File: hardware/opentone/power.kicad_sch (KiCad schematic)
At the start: 32 parts

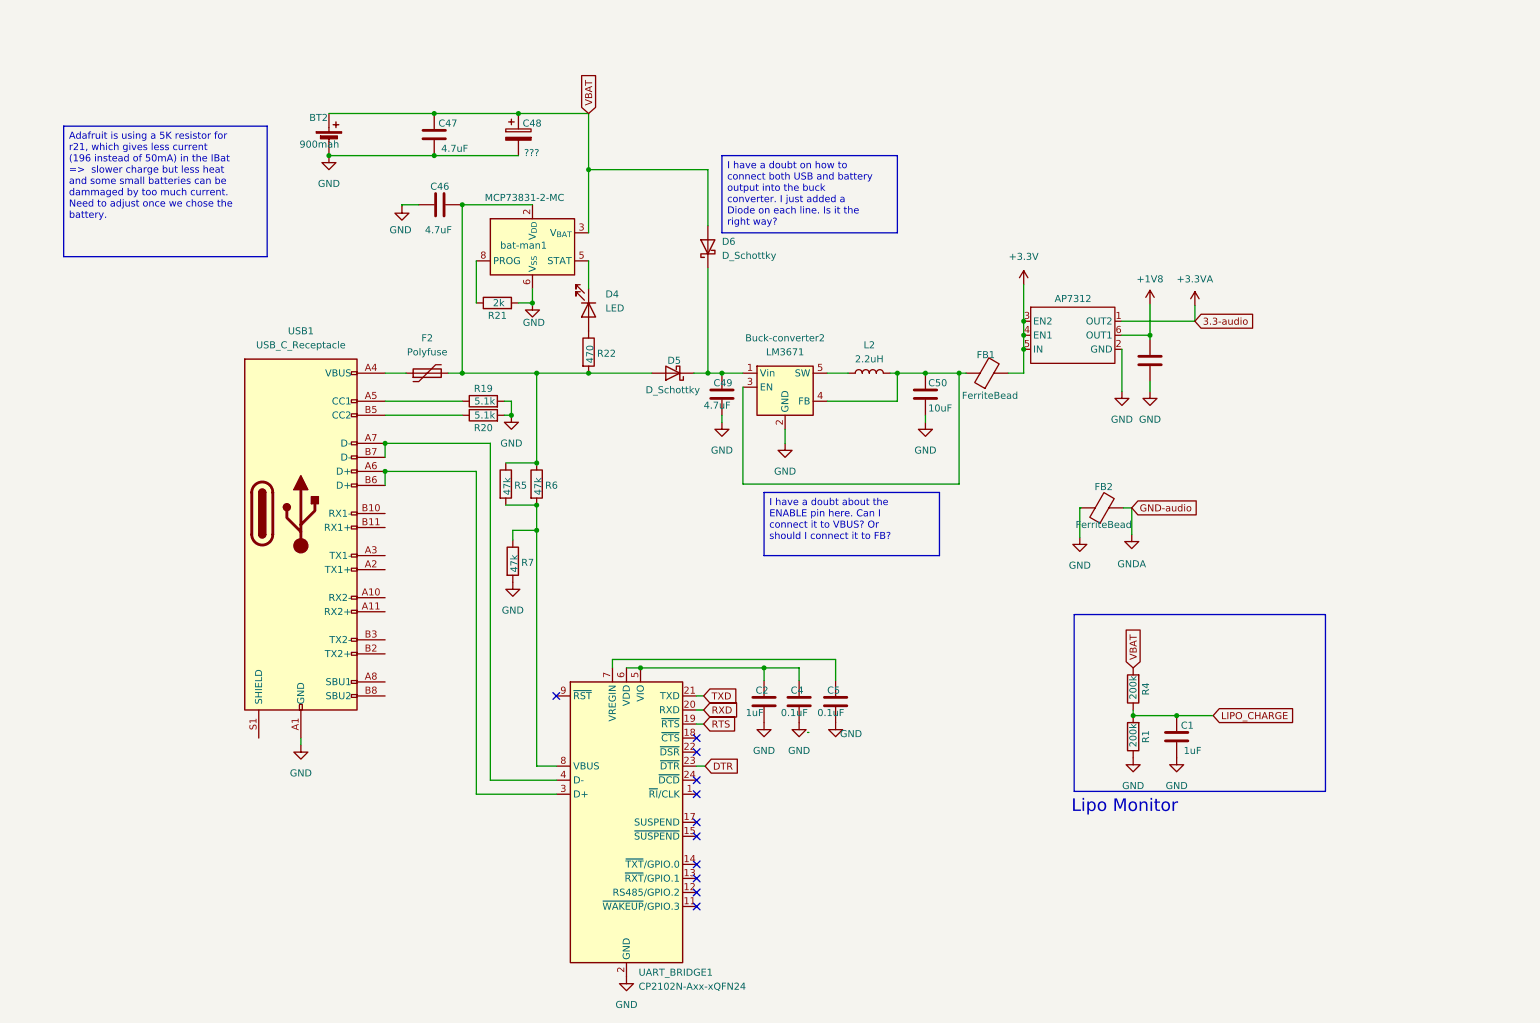
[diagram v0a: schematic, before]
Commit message: reworked power schematics
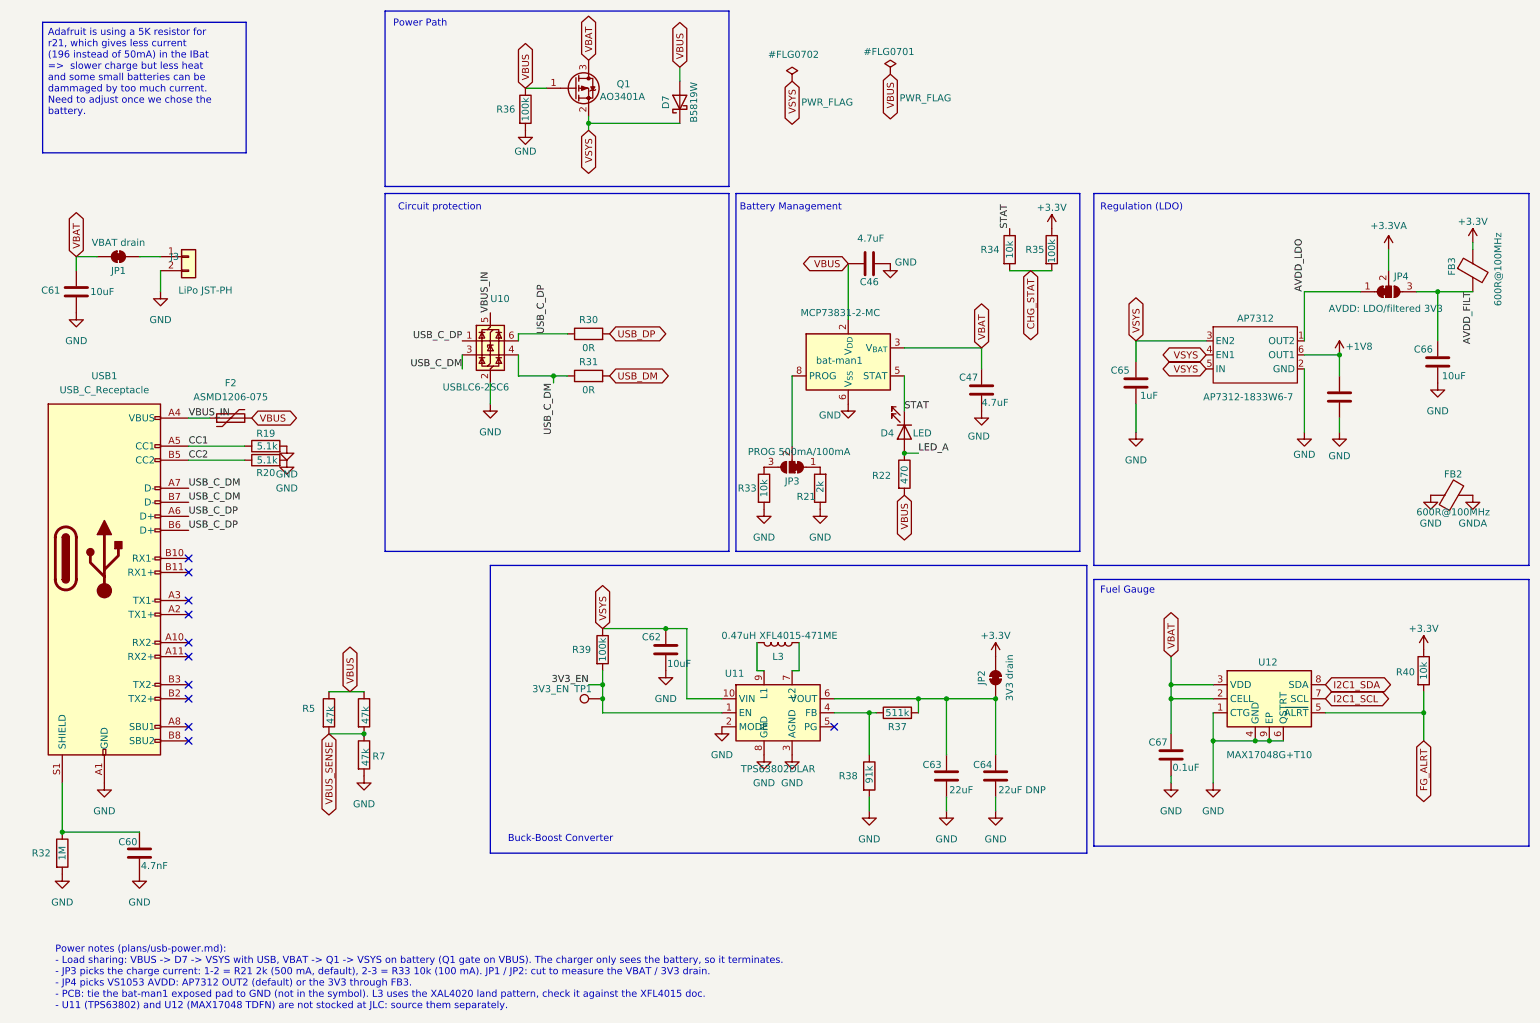
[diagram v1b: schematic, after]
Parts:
- removed BT2: 900mah, symbol Device:Battery_Cell
- removed Buck-converter2: LM3671, Package_TO_SOT_SMD:TSOT-23-5, symbol Regulator_Switching:LM3670MF
- removed C1, C2: 1uF, symbol Device:C
- removed C4, C5: 0.1uF, symbol Device:C
- removed C48: ???, symbol Device:C_Polarized
- removed C49: 4.7uF, symbol Device:C
- removed C50: 10uF, symbol Device:C
- removed D5, D6: D_Schottky, symbol Device:D_Schottky
- removed FB1: FerriteBead, symbol Device:FerriteBead
- removed L2: 2.2uH, symbol Device:L
- removed R1, R4: 200k, symbol Device:R
- removed UART_BRIDGE1: CP2102N-Axx-xQFN24, Package_DFN_QFN:QFN-24-1EP_4x4mm_P0.5mm_EP2.6x2.6mm, symbol Interface_USB:CP2102N-Axx-xQFN24
- added C60: 4.7nF, Capacitor_SMD:C_0805_2012Metric, symbol Device:C
- added C61, C62, C66: 10uF, Capacitor_SMD:C_0805_2012Metric, symbol Device:C
- added C63: 22uF, Capacitor_SMD:C_0805_2012Metric, symbol Device:C
- added C64: 22uF DNP, Capacitor_SMD:C_0805_2012Metric, symbol Device:C
- added C65: 1uF, Capacitor_SMD:C_0805_2012Metric, symbol Device:C
- added C67: 0.1uF, Capacitor_SMD:C_0805_2012Metric, symbol Device:C
- added D7: B5819W, Diode_SMD:D_SOD-123, symbol Device:D_Schottky
- added FB3: 600R@100MHz, Inductor_SMD:L_0805_2012Metric, symbol Device:FerriteBead
- added J3: LiPo JST-PH, Connector_JST:JST_PH_S2B-PH-SM4-TB_1x02-1MP_P2.00mm_Horizontal, symbol Connector_Generic:Conn_01x02
- added JP1: VBAT drain, Jumper:SolderJumper-2_P1.3mm_Bridged_RoundedPad1.0x1.5mm, symbol Jumper:SolderJumper_2_Bridged
- added JP2: 3V3 drain, Jumper:SolderJumper-2_P1.3mm_Bridged_RoundedPad1.0x1.5mm, symbol Jumper:SolderJumper_2_Bridged
- added JP3: PROG 500mA/100mA, Jumper:SolderJumper-3_P1.3mm_Bridged12_RoundedPad1.0x1.5mm, symbol Jumper:SolderJumper_3_Bridged12
- added JP4: AVDD: LDO/filtered 3V3, Jumper:SolderJumper-3_P1.3mm_Bridged12_RoundedPad1.0x1.5mm, symbol Jumper:SolderJumper_3_Bridged12
- added L3: 0.47uH XFL4015-471ME, Inductor_SMD:L_Coilcraft_XAL4020-XXX, symbol Device:L
- added Q1: AO3401A, Package_TO_SOT_SMD:SOT-23, symbol Transistor_FET:AO3401A
- added R30, R31: 0R, Resistor_SMD:R_0805_2012Metric, symbol Device:R
- added R32: 1M, Resistor_SMD:R_0805_2012Metric, symbol Device:R
- added R33, R34, R40: 10k, Resistor_SMD:R_0805_2012Metric, symbol Device:R
- added R35, R36, R39: 100k, Resistor_SMD:R_0805_2012Metric, symbol Device:R
- added R37: 511k, Resistor_SMD:R_0805_2012Metric, symbol Device:R
- added R38: 91k, Resistor_SMD:R_0805_2012Metric, symbol Device:R
- added TP1: 3V3_EN, TestPoint:TestPoint_Pad_D1.0mm, symbol Connector:TestPoint
- added U10: USBLC6-2SC6, Package_TO_SOT_SMD:SOT-23-6, symbol Power_Protection:USBLC6-2SC6
- added U11: TPS63802DLAR, opentone:Texas_DLA0010A_VSON-HR-10_2x3mm_P0.5mm, symbol opentone:TPS63802
- added U12: MAX17048G+T10, Package_DFN_QFN:TDFN-8-1EP_2x2mm_P0.5mm_EP0.8x1.2mm, symbol opentone:MAX17048
- AP7312: value ~ -> AP7312-1833W6-7
- C46, C47, C52: footprint (none) -> Capacitor_SMD:C_0805_2012Metric
- D4: footprint (none) -> LED_SMD:LED_0805_2012Metric
- F2: value Polyfuse -> ASMD1206-075; footprint (none) -> Fuse:Fuse_1206_3216Metric
- FB2: value FerriteBead -> 600R@100MHz; footprint (none) -> Inductor_SMD:L_0805_2012Metric
- R19, R20, R21, R22, R5, R6, R7: footprint (none) -> Resistor_SMD:R_0805_2012Metric
- USB1: footprint (none) -> Connector_USB:USB_C_Receptacle_HRO_TYPE-C-31-M-12
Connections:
- net +3.3V: now also FB3.1, JP2.2 (B), R35.1, R40.1; no longer AP7312.3 (EN2), AP7312.4 (EN1), AP7312.5 (IN)
- net +3.3VA: now also JP4.2 (C); no longer AP7312.1 (OUT2)
- net GND: now also R21.1, C60.2, C61.2, C62.2, C63.2, C64.2, C65.2, C66.2, C67.2, J3.2 (Pin_2), R32.2, R33.2, R36.2, R38.2, U10.2 (GND), U11.2 (MODE), U11.3 (AGND), U11.8 (GND), U12.1 (CTG), U12.4 (GND), U12.6 (QSTRT), U12.9 (EP); no longer R21.2
- net VBAT: now also C61.1, C67.1, JP1.2 (B), Q1.3 (D), U12.2 (CELL), U12.3 (VDD)
- net STAT: now reaches D4.1 (K), bat-man1.5 (STAT)
- net STAT: now also R34.1
- net LED_A: now reaches D4.2 (A), R22.1
- net VBUS_IN: now reaches F2.1, USB1.A4 (VBUS), USB1.A9 (VBUS), USB1.B4 (VBUS), USB1.B9 (VBUS)
- net VBUS_IN: now also U10.5 (VBUS)
- net VBUS: now reaches C46.2, F2.2, R22.2, R5.1, R6.1, bat-man1.1 (V_{DD}), bat-man1.2 (V_{DD})
- net VBUS: now also D7.2 (A), Q1.1 (G), R36.1
- net USB_C_DP: now reaches USB1.A6 (D+), USB1.B6 (D+)
- net USB_C_DP: now also R30.1, U10.1 (I/O1), U10.6 (I/O1)
- net USB_C_DM: now reaches USB1.A7 (D-), USB1.B7 (D-)
- net USB_C_DM: now also R31.1, U10.3 (I/O2), U10.4 (I/O2)
- net VBUS_SENSE: now reaches R5.2, R6.2, R7.1
- net CC1: now reaches R19.1, USB1.A5 (CC1)
- net CC2: now reaches R20.1, USB1.B5 (CC2)
- net at USB1.S1 (SHIELD): now also C60.1, R32.1
- net at bat-man1.8 (PROG): now also JP3.2 (C); no longer R21.1
- new net: R37.1, R38.1, U11.4 (FB)
- new net: C63.1, C64.1, JP2.1 (A), R37.2, U11.6 (VOUT)
- new net: L3.1, U11.7 (L2)
- new net: L3.2, U11.9 (L1)
- new net: JP3.3 (B), R33.1
- new net: JP3.1 (A), R21.2
- new net: J3.1 (Pin_1), JP1.1 (A)
- new net 3V3_EN: R39.2, TP1.1, U11.1 (EN)
- new net AVDD_FILT: C66.1, FB3.2, JP4.3 (B)
- new net AVDD_LDO: AP7312.1 (OUT2), JP4.1 (A)
- new net CHG_STAT: R34.2, R35.2
- new net FG_ALRT: R40.2, U12.5 (~{ALRT})
- new net I2C1_SCL: U12.7 (SCL)
- new net I2C1_SDA: U12.8 (SDA)
- new net USB_DM: R31.2
- new net USB_DP: R30.2
- new net VSYS: AP7312.3 (EN2), AP7312.4 (EN1), AP7312.5 (IN), C62.1, C65.1, D7.1 (K), Q1.2 (S), R39.1, U11.10 (VIN)
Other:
- note added: "Battery Management"
- note added: "Buck-Boost Converter"
- note added: "Circuit protection"
- note added: "Fuel Gauge"
- note added: "Power Path"
- note added: "Power notes (plans/usb-power.md): - Load sharing: VBUS -> D7 -> VSYS with USB, VBAT -> Q1 -> VSYS on battery (Q1 gate on VBUS). The charger only sees the battery, so it terminates. - JP3 picks the charge current: 1-2 = R21 2k (500 mA, default), 2-3 = R33 10k (100 mA). JP1 / JP2: cut to measure the VBAT / 3V3 drain. - JP4 picks VS1053 AVDD: AP7312 OUT2 (default) or the 3V3 through FB3. - PCB: tie 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"
- note added: "Regulation (LDO)"
- note removed: "Lipo Monitor"
- moved on the sheet: AP7312, C46, C47, D4, F2, FB2, R19, R20, R21, R22, R5, R7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

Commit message: updated buttons and MCU
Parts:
- R39: value 100k -> 470k
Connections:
- net 3V3_EN: now also AP7312.3 (EN2), AP7312.4 (EN1)
- net VSYS: no longer AP7312.3 (EN2), AP7312.4 (EN1)
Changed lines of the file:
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@@
 	(wire
 		(pts
-			(xy 212.09 72.39) (xy 224.79 72.39)
-		)
-		(stroke
-			(width 0)
-			(type default)
-		)
-	)
-	(wire
-		(pts
 			(xy 101.6 26.67) (xy 105.41 26.67)
 		)
@@
 	(wire
 		(pts
+			(xy 224.79 72.39) (xy 224.79 74.93)
+		)
+		(stroke
+			(width 0)
+			(type default)
+		)
+	)
+	(wire
+		(pts
 			(xy 266.7 63.5) (xy 262.89 63.5)
 		)
@@
 		)
 	)
-	(label "3V3_EN"
-		(at 113.03 134.62 180)
-		(effects
-			(font
-				(size 1.27 1.27)
-			)
-			(justify right bottom)
-		)
-	)
 	(label "USB_C_DM"
 		(at 40.64 101.6 0)
@@
 		)
 	)
+	(global_label "3V3_EN"
+		(shape input)
+		(at 113.03 134.62 180)
+		(fields_autoplaced yes)
+		(effects
+			(font
+				(size 1.27 1.27)
+			)
+			(justify right)
+		)
+		(property "Intersheetrefs" "${INTERSHEET_REFS}"
+			(at 113.03 134.62 0)
+			(effects
+				(font
+					(size 1.27 1.27)
+				)
+				(justify right)
+				(hide yes)
+			)
+		)
+	)
 	(global_label "USB_DP"
 		(shape bidirectional)
@@
 		)
 	)
-	(global_label "VSYS"
+	(global_label "3V3_EN"
 		(shape bidirectional)
 		(at 224.79 74.93 180)
@@
 			)
 		)
-		(property "Value" "100k"
+		(property "Value" "470k"
 			(at 115.57 128.27 90)
 			(effects
@@
 					(size 1.27 1.27)
 				)
+				(hide yes)
 			)
 		)

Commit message: added sd card, haptic, updated old parts and set a datasheet and MPN to all parts
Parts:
- removed AP7312: AP7312-1833W6-7, Package_TO_SOT_SMD:SOT-23-6, symbol opentone:AP7312
- removed FB2: 600R@100MHz, Inductor_SMD:L_0805_2012Metric, symbol Device:FerriteBead
- removed R6: 47k, Resistor_SMD:R_0805_2012Metric, symbol Device:R
- added C68, C69: 1uF, Capacitor_SMD:C_0603_1608Metric, symbol Device:C
- added JP6: VS1053 drain, Jumper:SolderJumper-2_P1.3mm_Bridged_RoundedPad1.0x1.5mm, symbol Jumper:SolderJumper_2_Bridged
- added NT1: GND-GNDA, NetTie:NetTie-2_SMD_Pad0.5mm, symbol Device:NetTie_2
- added R8: 100k, Resistor_SMD:R_0603_1608Metric, symbol Device:R
- added U13: TPS7A2033PDBVR, Package_TO_SOT_SMD:SOT-23-5, symbol Regulator_Linear:TLV73333PDBV
- added U14: TPS7A2018PDBVR, Package_TO_SOT_SMD:SOT-23-5, symbol Regulator_Linear:TLV73318PDBV
- C46, C47: LCSC (none) -> C1779; Manufacturer (none) -> Samsung Electro-Mechanics; Part number (none) -> CL21A475KAQNNNE
- C52, C65: footprint Capacitor_SMD:C_0805_2012Metric -> Capacitor_SMD:C_0603_1608Metric; LCSC (none) -> C15849; Manufacturer (none) -> Samsung Electro-Mechanics; Part number (none) -> CL10A105KB8NNNC
- C60: footprint Capacitor_SMD:C_0805_2012Metric -> Capacitor_SMD:C_0603_1608Metric; LCSC (none) -> C53987; Manufacturer (none) -> FH (Guangdong Fenghua); Part number (none) -> 0603B472K500NT
- C61, C62: LCSC (none) -> C15850; Manufacturer (none) -> Samsung Electro-Mechanics; Part number (none) -> CL21A106KAYNNNE
- C63, C64: LCSC (none) -> C45783; Manufacturer (none) -> Samsung Electro-Mechanics; Part number (none) -> CL21A226MAQNNNE
- C66: footprint Capacitor_SMD:C_0805_2012Metric -> Capacitor_SMD:C_0603_1608Metric; LCSC (none) -> C19702; Manufacturer (none) -> Samsung Electro-Mechanics; Part number (none) -> CL10A106KP8NNNC
- C67: footprint Capacitor_SMD:C_0805_2012Metric -> Capacitor_SMD:C_0603_1608Metric; LCSC (none) -> C14663; Manufacturer (none) -> YAGEO; Part number (none) -> CC0603KRX7R9BB104
- D4: footprint LED_SMD:LED_0805_2012Metric -> LED_SMD:LED_0603_1608Metric; LCSC (none) -> C2286; Manufacturer (none) -> Hubei KENTO Elec; Part number (none) -> KT-0603R
- D7: LCSC (none) -> C8598; Manufacturer (none) -> Jiangsu Changjing Electronics; Part number (none) -> B5819W SL
- F2: LCSC (none) -> C135339; Manufacturer (none) -> Shenzhen JDT Fuse; Part number (none) -> ASMD1206-075
- FB3: footprint Inductor_SMD:L_0805_2012Metric -> Inductor_SMD:L_0603_1608Metric; LCSC (none) -> C1002; Manufacturer (none) -> Sunlord; Part number (none) -> GZ1608D601TF
- J3: LCSC (none) -> C295747; Manufacturer (none) -> JST; Part number (none) -> S2B-PH-SM4-TB(LF)(SN)
- JP1, JP2, JP3, JP4, TP1: now left out of the parts list
- L3: value 0.47uH XFL4015-471ME -> 0.47uH DFE252012P-R47M; footprint Inductor_SMD:L_Coilcraft_XAL4020-XXX -> Inductor_SMD:L_1008_2520Metric_Pad1.43x2.20mm_HandSolder; LCSC (none) -> C237552; Manufacturer (none) -> Murata Electronics; Part number (none) -> DFE252012P-R47M=P2
- Q1: LCSC (none) -> C15127; Manufacturer (none) -> Alpha & Omega Semiconductor; Part number (none) -> AO3401A
- R19, R20: footprint Resistor_SMD:R_0805_2012Metric -> Resistor_SMD:R_0603_1608Metric; LCSC (none) -> C23186; Manufacturer (none) -> UNI-ROYAL; Part number (none) -> 0603WAF5101T5E
- R21: footprint Resistor_SMD:R_0805_2012Metric -> Resistor_SMD:R_0603_1608Metric; LCSC (none) -> C22975; Manufacturer (none) -> UNI-ROYAL; Part number (none) -> 0603WAF2001T5E
- R22: footprint Resistor_SMD:R_0805_2012Metric -> Resistor_SMD:R_0603_1608Metric; LCSC (none) -> C23179; Manufacturer (none) -> UNI-ROYAL; Part number (none) -> 0603WAF4700T5E
- R30, R31: footprint Resistor_SMD:R_0805_2012Metric -> Resistor_SMD:R_0603_1608Metric; LCSC (none) -> C21189; Manufacturer (none) -> UNI-ROYAL; Part number (none) -> 0603WAF0000T5E
- R32: footprint Resistor_SMD:R_0805_2012Metric -> Resistor_SMD:R_0603_1608Metric; LCSC (none) -> C22935; Manufacturer (none) -> UNI-ROYAL; Part number (none) -> 0603WAF1004T5E
- R33, R40: footprint Resistor_SMD:R_0805_2012Metric -> Resistor_SMD:R_0603_1608Metric; LCSC (none) -> C25804; Manufacturer (none) -> UNI-ROYAL; Part number (none) -> 0603WAF1002T5E
- R34: value 10k -> 100k; footprint Resistor_SMD:R_0805_2012Metric -> Resistor_SMD:R_0603_1608Metric; LCSC (none) -> C25803; Manufacturer (none) -> UNI-ROYAL; Part number (none) -> 0603WAF1003T5E
- R35: value 100k -> 1M; footprint Resistor_SMD:R_0805_2012Metric -> Resistor_SMD:R_0603_1608Metric; LCSC (none) -> C22935; Manufacturer (none) -> UNI-ROYAL; Part number (none) -> 0603WAF1004T5E
- R36: footprint Resistor_SMD:R_0805_2012Metric -> Resistor_SMD:R_0603_1608Metric; LCSC (none) -> C25803; Manufacturer (none) -> UNI-ROYAL; Part number (none) -> 0603WAF1003T5E
- R37: footprint Resistor_SMD:R_0805_2012Metric -> Resistor_SMD:R_0603_1608Metric; LCSC (none) -> C227946; Manufacturer (none) -> YAGEO; Part number (none) -> AC0603FR-07511KL
- R38: footprint Resistor_SMD:R_0805_2012Metric -> Resistor_SMD:R_0603_1608Metric; LCSC (none) -> C137671; Manufacturer (none) -> YAGEO; Part number (none) -> RC0603FR-0791KL
- R39: footprint Resistor_SMD:R_0805_2012Metric -> Resistor_SMD:R_0603_1608Metric; LCSC (none) -> C23178; Manufacturer (none) -> UNI-ROYAL; Part number (none) -> 0603WAF4703T5E
- R5: footprint Resistor_SMD:R_0805_2012Metric -> Resistor_SMD:R_0603_1608Metric; LCSC (none) -> C25819; Manufacturer (none) -> UNI-ROYAL; Part number (none) -> 0603WAF4702T5E
- R7: value 47k -> 100k; footprint Resistor_SMD:R_0805_2012Metric -> Resistor_SMD:R_0603_1608Metric; LCSC (none) -> C25803; Manufacturer (none) -> UNI-ROYAL; Part number (none) -> 0603WAF1003T5E
- U10: LCSC (none) -> C7519; Manufacturer (none) -> STMicroelectronics; Part number (none) -> USBLC6-2SC6
- U11: Manufacturer (none) -> Texas Instruments; Part number (none) -> TPS63802DLAR
- U12: Manufacturer (none) -> Analog Devices; Part number (none) -> MAX17048G+T10
- USB1: LCSC (none) -> C165948; Manufacturer (none) -> Korean Hroparts Elec; Part number (none) -> TYPE-C-31-M-12
- bat-man1: LCSC (none) -> C150772; Manufacturer (none) -> Microchip; Part number (none) -> MCP73831-2ACI/MC
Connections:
- net +1V8: now also C69.1, U14.5 (OUT); no longer C52.1
- net AVDD_LDO: now also C52.1, U13.5 (OUT)
- net GND: now also C68.2, C69.2, NT1.1, R8.2, U13.2 (GND), U14.2 (GND)
- net GNDA: now also NT1.2
- net VSYS: now also JP6.1 (A); no longer C65.1
- net 3V3_FB: now reaches R37.1, R38.1, U11.4 (FB)
- net 3V3_REG: now reaches C63.1, C64.1, JP2.1 (A), R37.2, U11.6 (VOUT)
- net PROG_10K: now reaches JP3.3 (B), R33.1
- net PROG_2K: now reaches JP3.1 (A), R21.2
- net PROG: now reaches JP3.2 (C), bat-man1.8 (PROG)
- new net VS_EN: R8.1, U13.3 (EN), U14.3 (EN)
- new net VS_VIN: C65.1, C68.1, JP6.2 (B), U13.1 (IN), U14.1 (IN)
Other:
- note added: "Power notes (plans/usb-power.md): - Load sharing: VBUS -> D7 -> VSYS with USB, VBAT -> Q1 -> VSYS on battery (Q1 gate on VBUS). The charger only sees the battery, so it terminates. - JP3 picks the charge current: 1-2 = R21 2k (500 mA, default), 2-3 = R33 10k (100 mA). JP1 / JP2: cut to measure the VBAT / 3V3 drain. - U13 TPS7A2033 (3.3 V) + U14 TPS7A2018 (1.8 V) = VS1053 only (+3.3VA analog + IO,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"
- note removed: "Power notes (plans/usb-power.md): - Load sharing: VBUS -> D7 -> VSYS with USB, VBAT -> Q1 -> VSYS on battery (Q1 gate on VBUS). The charger only sees the battery, so it terminates. - JP3 picks the charge current: 1-2 = R21 2k (500 mA, default), 2-3 = R33 10k (100 mA). JP1 / JP2: cut to measure the VBAT / 3V3 drain. - JP4 picks VS1053 AVDD: AP7312 OUT2 (default) or the 3V3 through FB3. - PCB: tie 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"
- moved on the sheet: C65, C66, FB3, JP4

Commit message: added recommendations from Teel s checklists
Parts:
- added D8: SMF5.0A, Diode_SMD:D_SOD-123F, symbol Device:D_Zener
- added Q2: AO3401A, Package_TO_SOT_SMD:SOT-23, symbol Transistor_FET:AO3401A
- added R6: 100k, Resistor_SMD:R_0603_1608Metric, symbol Device:R
- added TP2: VSYS, TestPoint:TestPoint_Pad_D1.0mm, symbol Connector:TestPoint
- added TP3: VBAT, TestPoint:TestPoint_Pad_D1.0mm, symbol Connector:TestPoint
- added TP4: +3.3V, TestPoint:TestPoint_Pad_D1.0mm, symbol Connector:TestPoint
- added TP5: +1V8, TestPoint:TestPoint_Pad_D1.0mm, symbol Connector:TestPoint
- added TP6: +3.3VA, TestPoint:TestPoint_Pad_D1.0mm, symbol Connector:TestPoint
- bat-man1: symbol Battery_Management:MCP73831-2-MC -> opentone:MCP73831-2-MC_EP
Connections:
- net +1V8: now also TP5.1
- net +3.3V: now also TP4.1
- net +3.3VA: now also TP6.1
- net GND: now also bat-man1.9, D8.2 (A), R6.2
- net VBAT: now also TP3.1
- net VBUS: now also D8.1 (K)
- net VSYS: now also TP2.1
- net at JP1.1 (A): now also Q2.2 (S); no longer J3.1 (Pin_1)
- new net: Q2.1 (G), R6.1
- new net: J3.1 (Pin_1), Q2.3 (D)
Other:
- note added: "Power notes (plans/usb-power.md): - Load sharing: VBUS -> D7 -> VSYS with USB, VBAT -> Q1 -> VSYS on battery (Q1 gate on VBUS). The charger only sees the battery, so it terminates. - Q2: battery reverse-polarity guard (drain on J3, gate to GND via R6). The gauge reads ~5-30 mV off under load. - JP3 picks the charge current: 1-2 = R21 2k (500 mA, default), 2-3 = R33 10k (100 mA). JP1 / JP2: cut to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"
- note removed: "Power notes (plans/usb-power.md): - Load sharing: VBUS -> D7 -> VSYS with USB, VBAT -> Q1 -> VSYS on battery (Q1 gate on VBUS). The charger only sees the battery, so it terminates. - JP3 picks the charge current: 1-2 = R21 2k (500 mA, default), 2-3 = R33 10k (100 mA). JP1 / JP2: cut to measure the VBAT / 3V3 drain. - U13 TPS7A2033 (3.3 V) + U14 TPS7A2018 (1.8 V) = VS1053 only (+3.3VA analog + IO,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"
- moved on the sheet: J3

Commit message: DAC
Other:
- moved on the sheet: Q2
